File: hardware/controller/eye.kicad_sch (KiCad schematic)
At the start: 25 parts, among them U4 baochip1x, U5 EMS4000RSW, Y1 48 MHz

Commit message: tidying up schematic and drawing outline for board
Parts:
- renumbered C13 to C11, C14 to C12, C22 to C13, C15 to C14, C18 to C15, C20 to C16, C16 to C17, C17 to C18, C11 to C19, C19 to C20, C12 to C22, R21 to R10, R19 to R11, R20 to R12, R18 to R8, R17 to R9, U5 to U4, U4 to U5

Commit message: welcome to the pcb, parts
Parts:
- TP1, TP2: now left out of the parts list
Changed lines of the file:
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@@
 		(body_style 1)
 		(exclude_from_sim no)
-		(in_bom yes)
-		(on_board yes)
-		(in_pos_files yes)
+		(in_bom no)
+		(on_board yes)
+		(in_pos_files no)
 		(dnp no)
 		(fields_autoplaced yes)
@@
 		(body_style 1)
 		(exclude_from_sim no)
-		(in_bom yes)
-		(on_board yes)
-		(in_pos_files yes)
+		(in_bom no)
+		(on_board yes)
+		(in_pos_files no)
 		(dnp no)
 		(fields_autoplaced yes)

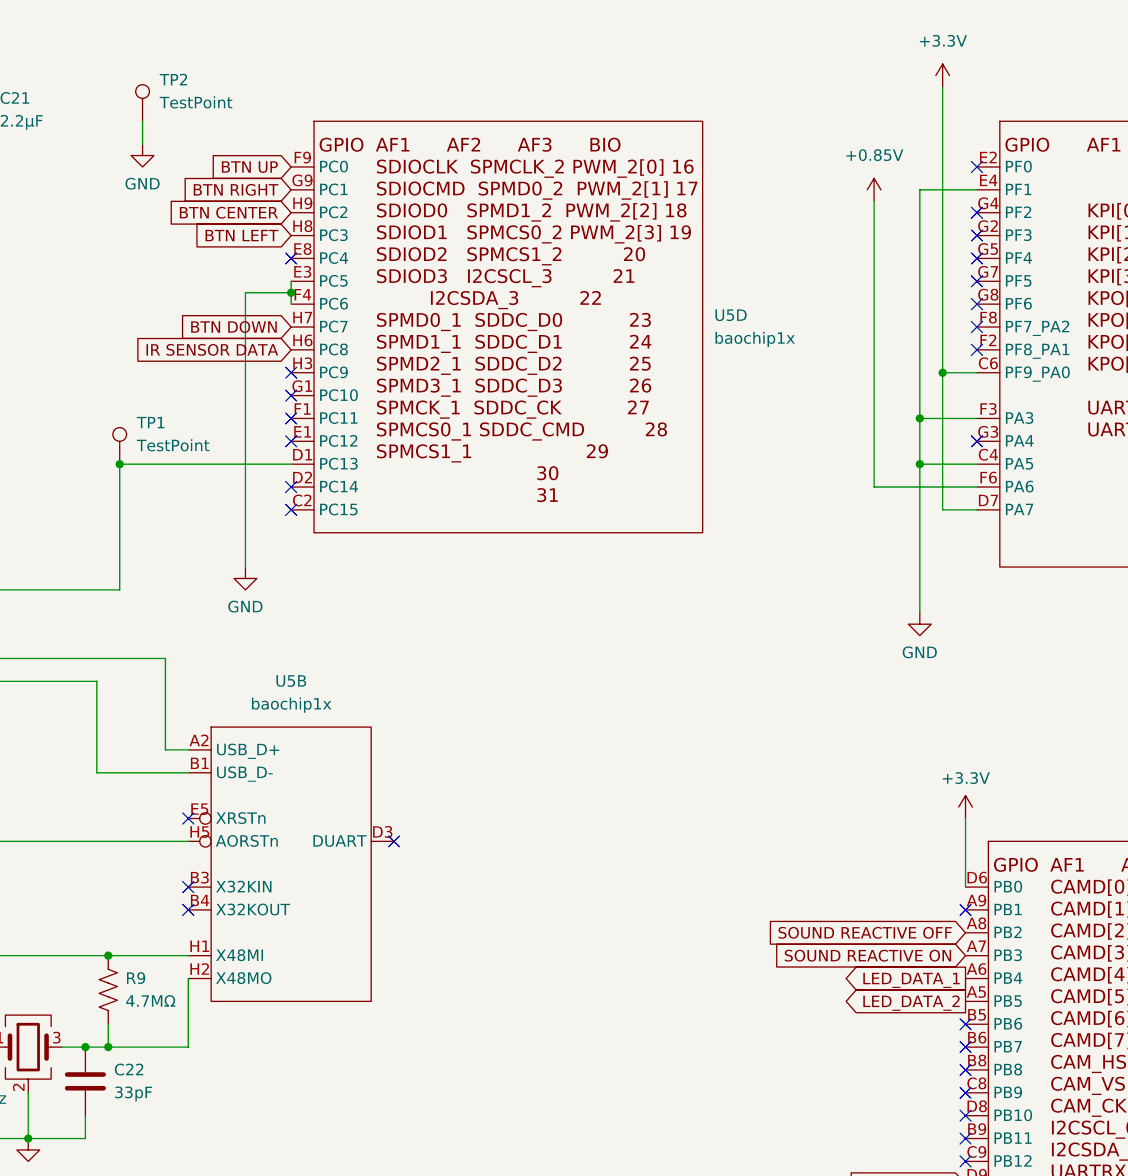
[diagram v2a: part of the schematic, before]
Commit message: everything routed
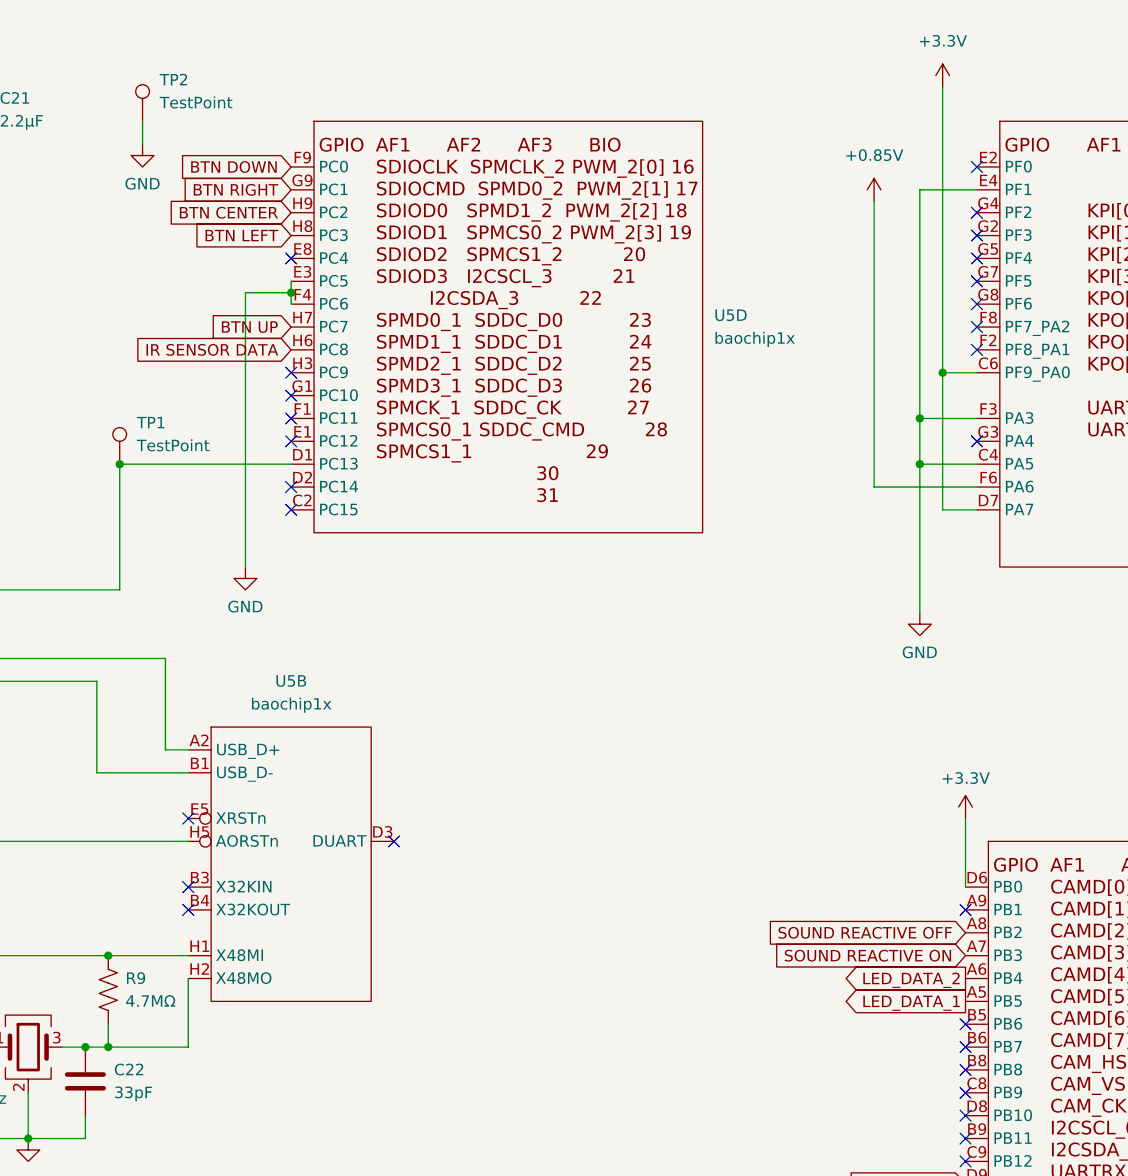
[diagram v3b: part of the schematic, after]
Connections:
- net BTN DOWN: now also U5.F9 (PC0); no longer U5.H7 (PC7)
- net BTN UP: now also U5.H7 (PC7); no longer U5.F9 (PC0)
- net LED_DATA_1: now also U5.A5 (PB5); no longer U5.A6 (PB4)
- net LED_DATA_2: now also U5.A6 (PB4); no longer U5.A5 (PB5)
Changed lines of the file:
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@@
 		)
 	)
-	(global_label "LED_DATA_1"
+	(global_label "LED_DATA_2"
 		(shape output)
 		(at 222.25 119.38 180)
@@
 		)
 	)
-	(global_label "BTN UP"
+	(global_label "BTN DOWN"
 		(shape input)
 		(at 147.32 29.21 180)
@@
 		)
 	)
-	(global_label "LED_DATA_2"
+	(global_label "LED_DATA_1"
 		(shape output)
 		(at 222.25 121.92 180)
@@
 		)
 	)
-	(global_label "BTN DOWN"
+	(global_label "BTN UP"
 		(shape input)
 		(at 147.32 46.99 180)

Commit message: routing adjustments/fixes
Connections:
- net LED_DATA_1: now also U5.G1 (PC10); no longer U5.A5 (PB5)
- net LED_DATA_2: now also U5.H3 (PC9); no longer U5.A6 (PB4)
- net SOUND REACTIVE OFF: now also U5.F1 (PC11); no longer U5.A8 (PB2)
- net SOUND REACTIVE ON: now also U5.E1 (PC12); no longer U5.A7 (PB3)
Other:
- moved on the sheet: TP1
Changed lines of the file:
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@@
 	)
 	(junction
-		(at 128.27 62.23)
+		(at 134.62 62.23)
 		(diameter 0)
 		(color 0 0 0 0)
@@
 	)
 	(no_connect
-		(at 147.32 59.69)
+		(at 222.25 116.84)
 	)
 	(no_connect
@@
 	)
 	(no_connect
-		(at 147.32 54.61)
+		(at 222.25 121.92)
 	)
 	(no_connect
@@
 	)
 	(no_connect
-		(at 147.32 57.15)
+		(at 222.25 114.3)
 	)
 	(no_connect
@@
 	)
 	(no_connect
-		(at 147.32 52.07)
+		(at 222.25 119.38)
 	)
 	(no_connect
@@
 	(wire
 		(pts
-			(xy 128.27 62.23) (xy 147.32 62.23)
+			(xy 128.27 62.23) (xy 134.62 62.23)
+		)
+		(stroke
+			(width 0)
+			(type default)
+		)
+	)
+	(wire
+		(pts
+			(xy 134.62 62.23) (xy 147.32 62.23)
 		)
 		(stroke
@@
 	(global_label "LED_DATA_2"
 		(shape output)
-		(at 222.25 119.38 180)
+		(at 147.32 52.07 180)
 		(fields_autoplaced yes)
 		(effects
@@
 		)
 		(property "Intersheetrefs" "${INTERSHEET_REFS}"
-			(at 208.2582 119.38 0)
+			(at 133.33 52.07 0)
 			(hide yes)
 			(show_name no)
@@
 	(global_label "SOUND REACTIVE ON"
 		(shape input)
-		(at 222.25 116.84 180)
+		(at 147.32 59.69 180)
 		(fields_autoplaced yes)
 		(effects
@@
 		)
 		(property "Intersheetrefs" "${INTERSHEET_REFS}"
-			(at 199.61 116.84 0)
+			(at 124.68 59.69 0)
 			(hide yes)
 			(show_name no)
@@
 	(global_label "LED_DATA_1"
 		(shape output)
-		(at 222.25 121.92 180)
+		(at 147.32 54.61 180)
 		(fields_autoplaced yes)
 		(effects
@@
 		)
 		(property "Intersheetrefs" "${INTERSHEET_REFS}"
-			(at 208.2582 121.92 0)
+			(at 133.33 54.61 0)
 			(hide yes)
 			(show_name no)
@@
 	(global_label "SOUND REACTIVE OFF"
 		(shape input)
-		(at 222.25 114.3 180)
+		(at 147.32 57.15 180)
 		(fields_autoplaced yes)
 		(effects
@@
 		)
 		(property "Intersheetrefs" "${INTERSHEET_REFS}"
-			(at 198.7633 114.3 0)
+			(at 123.83 57.15 0)
 			(hide yes)
 			(show_name no)
@@
 	(symbol
 		(lib_id "Connector:TestPoint")
-		(at 128.27 62.23 0)
+		(at 134.62 62.23 180)
 		(unit 1)
 		(body_style 1)
@@
 		(fields_autoplaced yes)
 		(property "Reference" "TP1"
-			(at 130.175 57.6579 0)
+			(at 134.62 67.6 0)
 			(show_name no)
 			(do_not_autoplace no)
@@
 					(size 1.27 1.27)
 				)
-				(justify left)
 			)
 		)
 		(property "Value" "TestPoint"
-			(at 130.175 60.1979 0)
+			(at 134.62 70.1 0)
 			(show_name no)
 			(do_not_autoplace no)
@@
 					(size 1.27 1.27)
 				)
-				(justify left)
 			)
 		)
 		(property "Footprint" "TestPoint:TestPoint_Pad_D1.0mm"
-			(at 133.35 62.23 0)
+			(at 139.7 62.23 0)
 			(hide yes)
 			(show_name no)
@@
 		)
 		(property "Datasheet" ""
-			(at 133.35 62.23 0)
+			(at 139.7 62.23 0)
 			(hide yes)
 			(show_name no)
@@
 		)
 		(property "Description" "test point"
-			(at 128.27 62.23 0)
+			(at 134.62 62.23 0)
 			(hide yes)
 			(show_name no)
